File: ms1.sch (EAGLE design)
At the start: 149 parts, among them IC1 MAX3232EUE, IC2 MAX3380EEUP, J1 POWERPOLE_POWER25A, J10 Radio, J11 A3, J12 A4, J13 A5, J14 A6, J15 A7, J16 D1, J17 D2, J18 D3, J19 D4, J2 ON, J20 D5, J21 D6, J22 D7, J3 LED-EN, J4 RS232, J5 RS485, J6 A1, J7 I2C, J8 A2, J9 TTL_SERIAL, Q1 DMG6602SVT, Q2 DMG6602SVT, Q3 DMG6602SVT, Q4 DMG6602SVT, U1 LT1934ES6TRMPBF, U2 LT1934ES6TRMPBF, U3 DS3231SN, U4 ISL3179EIBZ, X1 KUSBVX-BS1N

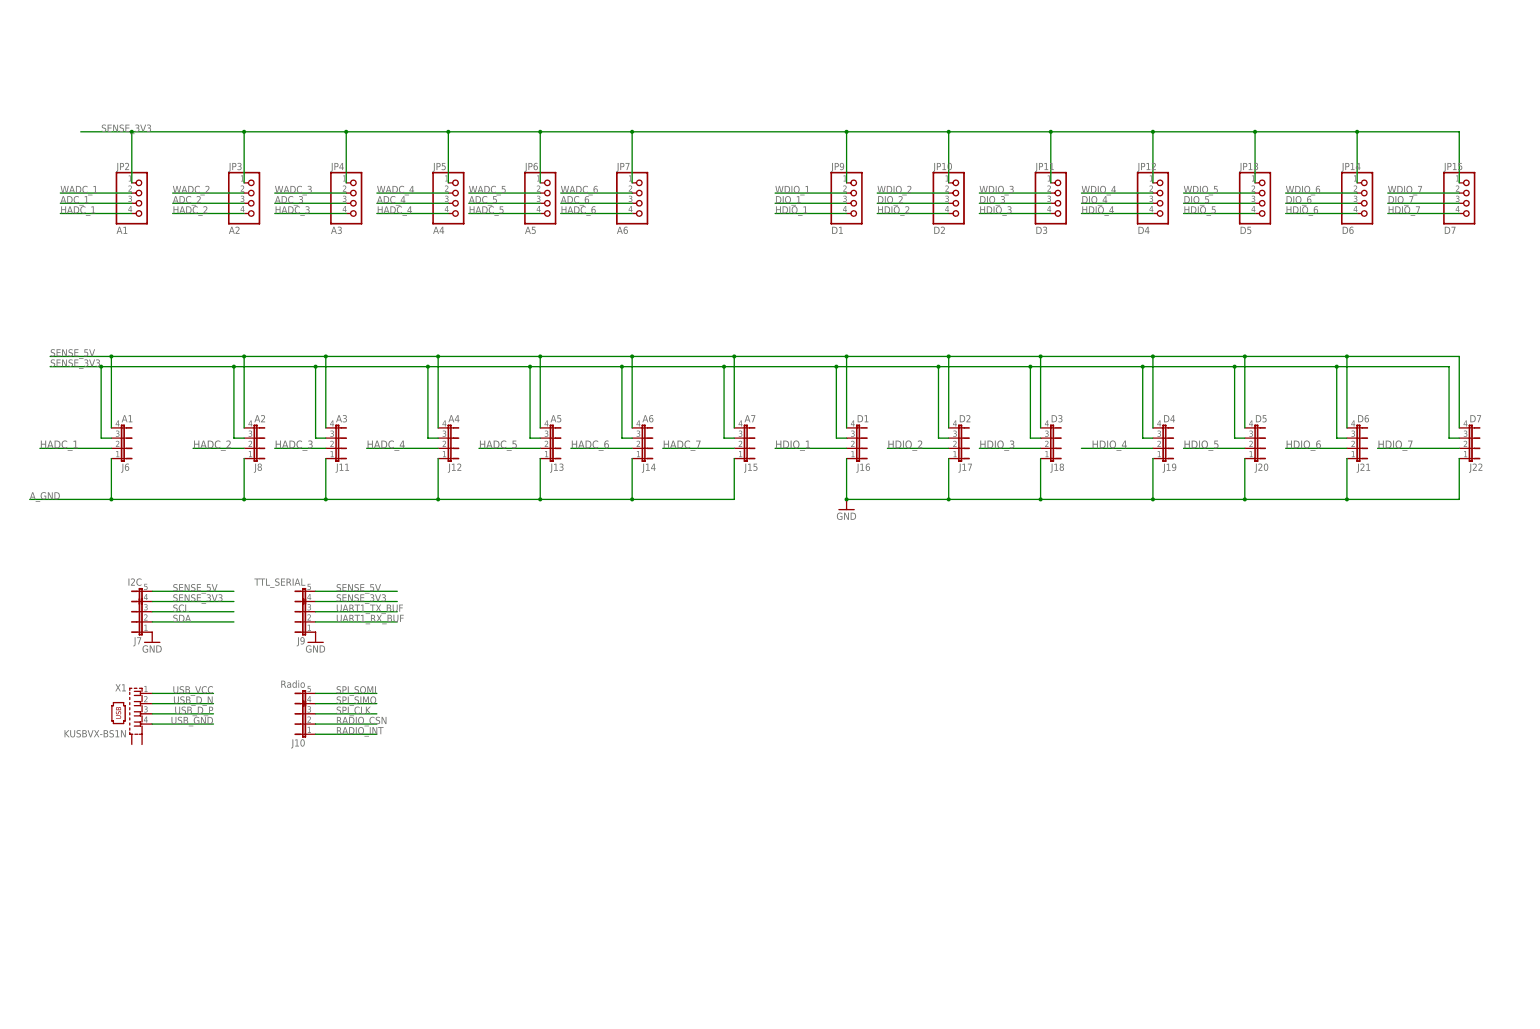
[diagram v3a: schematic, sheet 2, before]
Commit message: now uses correct serial buffer
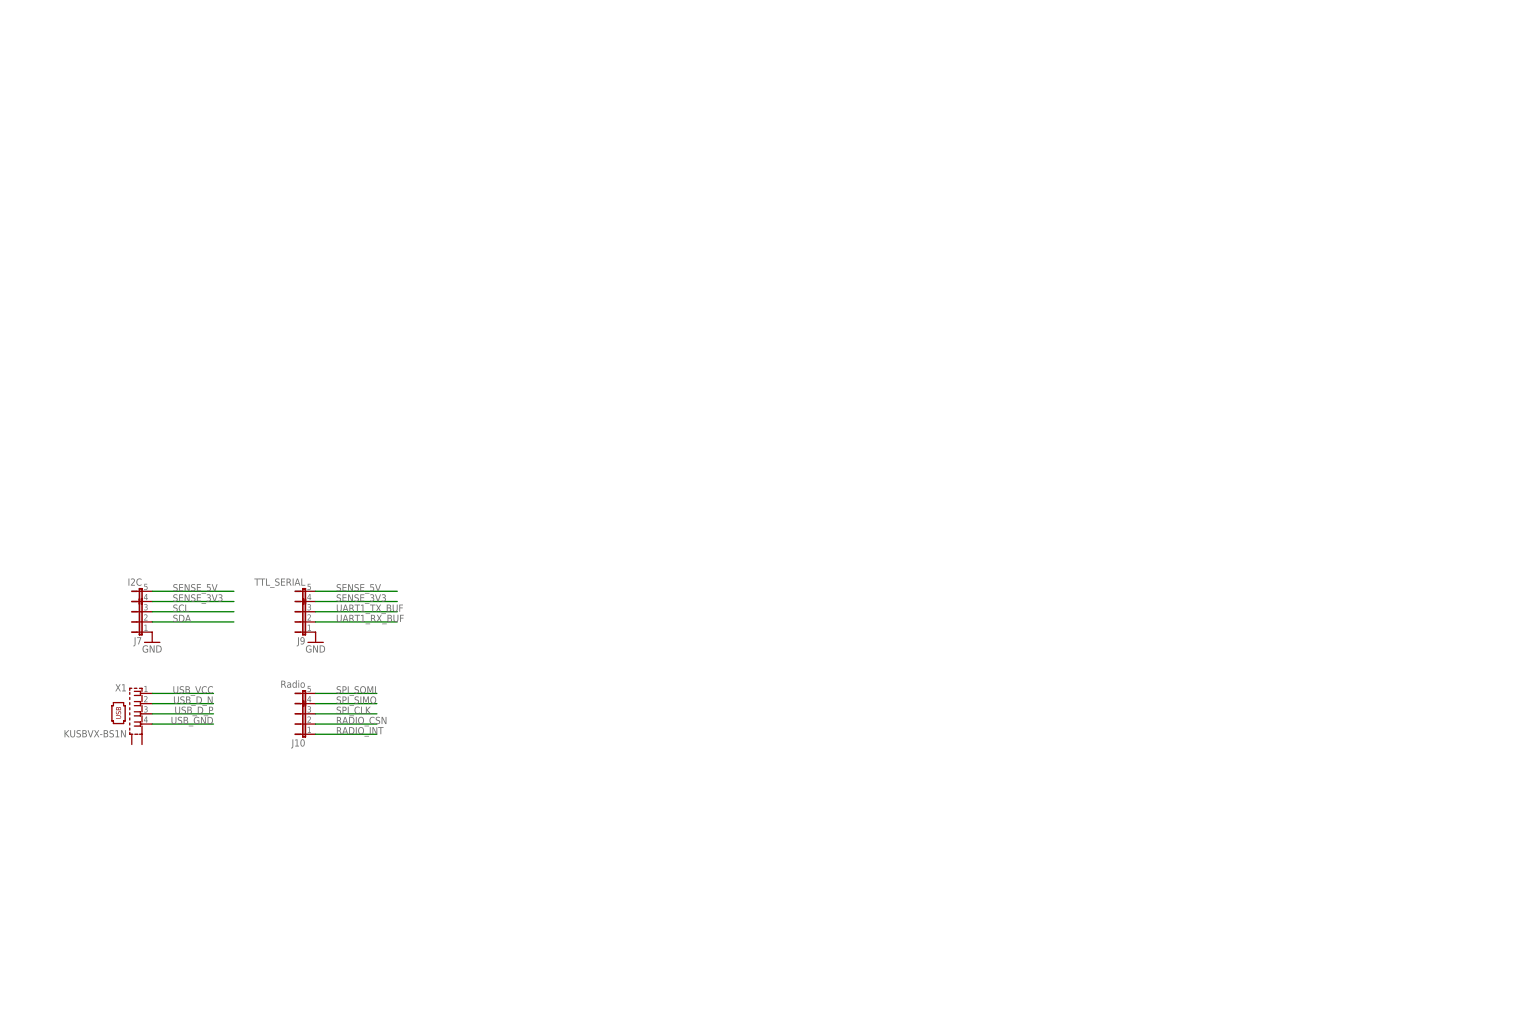
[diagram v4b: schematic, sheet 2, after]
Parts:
- removed C17, C18, C22, C23: 0.1uF, resistor:CPOL-EUA/3216-18W
- removed C26: 100nF, resistor:C-EUC0805
- removed IC2: MAX3380EEUP, basestation:MAX3380EEUP
- removed J11: A3, farnell-parts:4-PIN-MOLEX
- removed J12: A4, farnell-parts:4-PIN-MOLEX
- removed J13: A5, farnell-parts:4-PIN-MOLEX
- removed J14: A6, farnell-parts:4-PIN-MOLEX
- removed J15: A7, farnell-parts:4-PIN-MOLEX
- removed J16: D1, farnell-parts:4-PIN-MOLEX
- removed J17: D2, farnell-parts:4-PIN-MOLEX
- removed J18: D3, farnell-parts:4-PIN-MOLEX
- removed J19: D4, farnell-parts:4-PIN-MOLEX
- removed J20: D5, farnell-parts:4-PIN-MOLEX
- removed J21: D6, farnell-parts:4-PIN-MOLEX
- removed J22: D7, farnell-parts:4-PIN-MOLEX
- removed J6: A1, farnell-parts:4-PIN-MOLEX
- removed J8: A2, farnell-parts:4-PIN-MOLEX
- removed JP10: D2, pinhead:PINHD-1X4
- removed JP11: D3, pinhead:PINHD-1X4
- removed JP12: D4, pinhead:PINHD-1X4
- removed JP13: D5, pinhead:PINHD-1X4
- removed JP14: D6, pinhead:PINHD-1X4
- removed JP15: D7, pinhead:PINHD-1X4
- removed JP3: A2, pinhead:PINHD-1X4
- removed JP4: A3, pinhead:PINHD-1X4
- removed JP5: A4, pinhead:PINHD-1X4
- removed JP6: A5, pinhead:PINHD-1X4
- removed JP7: A6, pinhead:PINHD-1X4
- removed JP9: D1, pinhead:PINHD-1X4
- removed UART1_RX, UART1_TX: TPB2,54, testpad:TPB2,54
- added R7: 47K, resistor:R-EU_R0805
- added U$4: TXS0108E, basestation:TXS0108E
- JP2: value A1 -> (none); device pinhead:PINHD-1X4 -> jumper:JP2E
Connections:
- removed net A_GND: J11.1, J12.1, J13.1, J14.1, J15.1, J6.1, J8.1
- removed net HADC_1: J6.2, JP2.4
- removed net HADC_2: J8.2, JP3.4
- removed net HADC_3: J11.2, JP4.4
- removed net HADC_4: J12.2, JP5.4
- removed net HADC_5: J13.2, JP6.4
- removed net HADC_6: J14.2, JP7.4
- removed net HADC_7: J15.2
- removed net HDIO_1: J16.2, JP9.4
- removed net HDIO_2: J17.2, JP10.4
- removed net HDIO_3: J18.2, JP11.4
- removed net HDIO_4: J19.2, JP12.4
- removed net HDIO_5: J20.2, JP13.4
- removed net HDIO_6: J21.2, JP14.4
- removed net HDIO_7: J22.2, JP15.4
- removed net N$64: C17.-, IC2G$1.C1-
- removed net N$82: C18.+, IC2G$1.C2+
- removed net N$83: C18.-, IC2G$1.C2-
- removed net N$84: C22.-, IC2G$1.V-
- removed net N$9: C23.+, IC2G$1.V+
- removed net WADC_1: JP2.2
- removed net WADC_2: JP3.2
- removed net WADC_3: JP4.2
- removed net WADC_4: JP5.2
- removed net WADC_5: JP6.2
- removed net WADC_6: JP7.2
- removed net WDIO_1: JP9.2
- removed net WDIO_2: JP10.2
- removed net WDIO_3: JP11.2
- removed net WDIO_4: JP12.2
- removed net WDIO_5: JP13.2
- removed net WDIO_6: JP14.2
- removed net WDIO_7: JP15.2
- new net 232_RX: IC1G$1.R1OUT, U$4.A2
- new net 232_TX: IC1G$1.T1IN, U$4.A4
- new net 323_3V3: C19.2, IC1P.VCC, JP2.3
- new net 485_3V3: C14.1, JP2.1, R32.2, U4.VCC
- new net 485_RX: U$4.A1, U4.RO
- new net 485_TX: U$4.A3, U4.DI
- net ADC_1: no longer JP2.3
- net ADC_2: no longer JP3.3
- net ADC_3: no longer JP4.3
- net ADC_4: no longer JP5.3
- net ADC_5: no longer JP6.3
- net ADC_6: no longer JP7.3
- net DIO_1: no longer JP9.3
- net DIO_2: no longer JP10.3
- net DIO_3: no longer JP11.3, U$2.CA0
- net DIO_4: no longer JP12.3
- net DIO_5: no longer JP13.3, U$2.CA1
- net DIO_6: no longer JP14.3, U$2.CA2
- net DIO_7: no longer JP15.3
- net GND: now also U$4.GND; no longer C22.+, C23.-, C26.2, IC2P.GND, J16.1, J17.1, J18.1, J19.1, J20.1, J21.1, J22.1
- net N$8: now also R7.1, U$4.OE; no longer C17.+, IC2G$1.C1+
- net SENSE_3V3: now also JP2.2, R7.2, U$4.VCCA; no longer C14.1, C19.2, IC1P.VCC, IC2G$1.VL, J11.3, J12.3, J13.3, J14.3, J15.3, J16.3, J17.3, J18.3, J19.3, J20.3, J21.3, J22.3, J6.3, J8.3, JP10.1, JP11.1, JP12.1, JP13.1, JP14.1, JP15.1, JP2.1, JP3.1, JP4.1, JP5.1, JP6.1, JP7.1, JP9.1, R32.2, U4.VCC
- net SENSE_5V: no longer J11.4, J12.4, J13.4, J14.4, J15.4, J16.4, J17.4, J18.4, J19.4, J20.4, J21.4, J22.4, J6.4, J8.4
- net UART1_RX: now also U$4.B1, U$4.B2; no longer IC2G$1.T2IN, UART1_RX.TP
- net UART1_RX_BUF: no longer IC1G$1.R1OUT, IC2G$1.T2OUT, U4.RO
- net UART1_TX: now also U$4.B3, U$4.B4; no longer IC2G$1.T1IN, UART1_TX.TP
- net UART1_TX_BUF: no longer IC1G$1.T1IN, IC2G$1.T1OUT, U4.DI
- net VCC_3V3: now also U$4.VCCB; no longer C26.1, IC2G$1.!FORCEOFF, IC2G$1.FORCEON, IC2P.VCC
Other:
- note added: "Buffer so that drivers don't draw power from comms line."
- note added: "Each one on seperate outputs so that they can be powered individually"
- note added: "Serial Driver Choice"
- note removed: "Gum Serial Level Shift"
- note removed: "I/O Patch"
- note removed: "IO"

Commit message: now has: * rain gauge input * 2 digital io * 2 analog io * poly fuses
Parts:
- removed LED3: D3, led:LEDCHIP-LED0805
- removed LED4: D4, led:LEDCHIP-LED0805
- removed LED5: D5, led:LEDCHIP-LED0805
- removed LED6: D6, led:LEDCHIP-LED0805
- removed R13, R15, R16, R17: 56, resistor:R-EU_R0805
- added J11, J12: 4-PIN-MOLEX, farnell-parts:4-PIN-MOLEX
- added J13, J14, J8: ADC2, farnell-parts:3-PIN-MOLEX
- added J6: ADC1, farnell-parts:3-PIN-MOLEX
- added R31: 100K, resistor:R-EU_R0805
- added U$5, U$6, U$7: MCF0805, farnell-parts:MCF0805
- J5: value RS485 -> 2-PIN-MOLEX; device farnell-parts:5-PIN-MOLEX -> farnell-parts:2-PIN-MOLEX
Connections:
- removed net ADC_3: U$2.ADC3
- removed net ADC_4: U$2.ADC4
- removed net ADC_5: U$2.ADC5
- removed net ADC_6: U$2.ADC6
- removed net DIO_3: R13.2
- removed net DIO_4: R15.2
- removed net DIO_5: R16.2
- removed net DIO_6: R17.2
- removed net DIO_7: R18.2
- removed net N$11: LED6.A, R17.1
- removed net N$18: LED4.A, R15.1
- removed net N$19: LED3.A, R13.1
- removed net N$21: LED5.A, R16.1
- removed net UART1_RX_BUF: J9.2
- removed net UART1_TX_BUF: J9.3
- new net N$17: J12.4, U$6.P$1
- new net N$26: J5.1, U$7.P$1
- new net N$9: J11.4, U$5.P$1
- new net RAIN: J5.2, R18.2, R31.2, U$2.CA2
- new net TTL_RX: J9.2, U$4.A3
- new net TTL_TX: J9.3, U$4.A6
- net 232_TX: now also U$4.A5; no longer U$4.A4
- net 485_TX: now also U$4.A4; no longer U$4.A3
- net ADC_1: now also J6.2
- net ADC_2: now also J8.2
- net AGND: now also J6.3, J8.3
- net DIO_1: now also J13.2, U$2.CA0, U$2.TA0
- net DIO_2: now also J14.2
- net GND: now also J11.1, J12.1, J13.3, J14.3, R31.1; no longer J5.1
- net LGND: no longer LED3.C, LED4.C, LED5.C, LED6.C
- net RS232_RXD: now also J12.2
- net RS232_TXD: now also J12.3
- net RS485_N: now also J11.2; no longer J5.2
- net RS485_P: now also J11.3; no longer J5.3
- net SENSE_3V3: now also J13.1, J14.1, J6.1, J8.1; no longer J5.4
- net SENSE_5V: now also U$5.P$2, U$6.P$2; no longer J5.6
- net UART1_RX: now also U$4.B3
- net UART1_TX: now also U$4.B5, U$4.B6; no longer U$4.B3
- net VCC_3V3: now also U$7.P$2
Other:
- note added: "Analog Inputs"
- note added: "Digital Inputs"

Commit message: now all routed :)
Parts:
- removed C29: (no value), resistor:C-EUC0805
- removed C30: (no value), resistor:CPOL-EUB/3528-21R
- removed J9: TTL_SERIAL, farnell-parts:5-PIN-MOLEX
- removed JP16, JP8: (no value), SparkFun-Passives:JUMPER-2SMD-NO
- removed L7, L8: 10mH, resistor:L-EUL3230M
- removed LED12: RADIO, led:LEDCHIP-LED0805
- removed LED13: RADIO_EN, led:LEDCHIP-LED0805
- removed LED14: BAT_EN, led:LEDCHIP-LED0805
- removed LED15: SENSE_EN, led:LEDCHIP-LED0805
- removed R30: 56, resistor:R-EU_R0805
- removed R31: 100K, resistor:R-EU_R0805
- removed R32, R33: 1K, resistor:R-EU_R0805
- removed U$1: BUTTON_CELL_NEW, gumsense:BUTTON_CELL_NEW
- removed U$2: Z1, z1:Z1
- removed U$4: TXS0108E, basestation:TXS0108E
- added C22: 0.1uF, resistor:CPOL-EUA/3216-18W
- added C23: 100nF, resistor:C-EUC0805
- added F1, F2, F4, F5, F6, F7, F8: MCF0805, farnell-parts:MCF0805
- added JP3: (no value), SparkFun-Passives:JUMPER-2SMD-NC
- added JP4: (no value), jumper:JP2E
- added L1: 47uH, farnell-parts:SRU1048
- added L2: 20uH, rcl:L-EU6000-XXX-RC
- added LED3: RAIN, led:LEDCHIP-LED0805
- added LED4: 12V, led:LEDCHIP-LED0805
- added LED5: 3V3, led:LEDCHIP-LED0805
- added LED6: SENSE, led:LEDCHIP-LED0805
- added R13: 100K, resistor:R-EU_R0805
- added R15, R16: 56, resistor:R-EU_R0805
- added R17: 560, resistor:R-EU_R0805
- added U$8: CC1120-HEADER-SMT, CC11x:CC1120-HEADER-SMT
- C1: value 2200uF -> 2.2uF; device rcl:CPOL-EUE5-13 -> resistor:C-EUC0805
- C10: value 10pF -> 1uF
- C11: value 68uF -> 100nF; device rcl:CPOL-EUE -> resistor:C-EUC0805
- C12: value 330uF -> 2.2uF; device rcl:CPOL-EUE5-8.5 -> resistor:C-EUC0805
- C13: value 100nF -> 0.22uF
- C14: value 100nF -> 10pF; device glacsweb:C-EUC0805 -> resistor:C-EUC0805
- C15: value 0.1uF -> 68uF; device resistor:CPOL-EUA/3216-18W -> rcl:CPOL-EUE
- C16: value 0.1uF -> 330uF; device resistor:CPOL-EUA/3216-18W -> rcl:CPOL-EUE5-8.5
- C2: value 2.2uF -> 0.22uF
- C20: value 0.1uF -> 100nF; device resistor:CPOL-EUA/3216-18W -> glacsweb:C-EUC0805
- C24, C25: value 100nF -> 0.1uF; device resistor:C-EUC0805 -> resistor:CPOL-EUA/3216-18W
- C3: value 0.22uF -> 2200uF; device resistor:C-EUC0805 -> rcl:CPOL-EUE5-13
- C5: value 1uF -> 100uF; device resistor:C-EUC0805 -> rcl:CPOL-EUE
- C6: value 100uF -> 330uF; device rcl:CPOL-EUE -> rcl:CPOL-EUE5-8.5
- C7: value 330uF -> (none); device rcl:CPOL-EUE5-8.5 -> resistor:C-EUC0805
- C8: value 2.2uF -> (none); device resistor:C-EUC0805 -> resistor:CPOL-EUB/3528-21R
- C9: value 0.22uF -> 100nF
- J10: value Radio -> RS485; device farnell-parts:5-PIN-MOLEX -> farnell-parts:4-PIN-MOLEX
- J11: value 4-PIN-MOLEX -> I2C; device farnell-parts:4-PIN-MOLEX -> farnell-parts:5-PIN-MOLEX
- J12: value 4-PIN-MOLEX -> TTL_SERIAL
- J13: value ADC2 -> Radio; device farnell-parts:3-PIN-MOLEX -> farnell-parts:5-PIN-MOLEX
- J14: value ADC2 -> RS232; device farnell-parts:3-PIN-MOLEX -> farnell-parts:4-PIN-MOLEX
- J2: value ON -> RAIN
- J3: value LED-EN -> ADC1; device farnell-parts:2-PIN-MOLEX -> farnell-parts:3-PIN-MOLEX
- J4: value RS232 -> ON; device farnell-parts:5-PIN-MOLEX -> farnell-parts:2-PIN-MOLEX
- J5: value 2-PIN-MOLEX -> D1; device farnell-parts:2-PIN-MOLEX -> farnell-parts:3-PIN-MOLEX
- J6: value ADC1 -> D2
- J7: value I2C -> ADC2; device farnell-parts:5-PIN-MOLEX -> farnell-parts:3-PIN-MOLEX
- J8: value ADC2 -> LED-EN; device farnell-parts:3-PIN-MOLEX -> farnell-parts:2-PIN-MOLEX
- JP1: device SparkFun-Passives:JUMPER-2SMD-NC -> SparkFun-Passives:JUMPER-2SMD-NO
- JP2: device jumper:JP2E -> SparkFun-Passives:JUMPER-2SMD-NO
- L3: value 47uH -> 10mH; device farnell-parts:SRU1048 -> resistor:L-EUL3230M
- L4: value 20uH -> 10mH; device rcl:L-EU6000-XXX-RC -> resistor:L-EUL3230M
- LED10: value SENSE -> BAT_EN
- LED11: value SENSE_5V -> SENSE_EN
- LED7: value D7 -> 5V
- LED8: value 12V -> RADIO
- LED9: value 3V3 -> RADIO_EN
- R10, R8: value 56 -> 100K
- R14, R26: value 100K -> 56
- R19: value 560 -> 56
- R2: value 100K -> 1M
- R20: value 56 -> 1M
- R21: value 56 -> 332K
- R22: value 100K -> 150
- R23: value 1M -> 56
- R24: value 332K -> 56
- R25: value 150 -> 56
- R27, R29: value 56 -> 1K
- R28: value 56 -> 47K
- R3: value 100K -> 604K
- R4: value 51K -> 100K
- R5: value 1M -> 100K
- R6: value 604K -> 100K
- R7: value 47K -> 100K
- R9: value 100K -> 51K
- U$3: value CC1120-HEADER-SMT -> BUTTON_CELL_NEW; device CC11x:CC1120-HEADER-SMT -> gumsense:BUTTON_CELL_NEW
- U$5: value MCF0805 -> Z1; device farnell-parts:MCF0805 -> z1:Z1
- U$6: value MCF0805 -> TXS0108E; device farnell-parts:MCF0805 -> basestation:TXS0108E
- renumbered C27 to C17, C28 to C18, U$7 to F3
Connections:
- new net N$11: F4.P$1, J12.4
- new net N$18: F1.P$2, J3.1
- new net N$19: F2.P$2, J7.1
- new net N$21: F7.P$2, J6.1
- new net N$22: F8.P$2, J5.1
- net 232_RX: now also U$6.A2; no longer U$4.A2
- net 232_TX: now also U$6.A5; no longer U$4.A5
- net 323_3V3: now also C23.2, JP4.3; no longer C19.2, JP2.3
- net 485_3V3: now also C20.1, JP4.1, R27.2; no longer C14.1, JP2.1, R32.2
- net 485_RX: now also U$6.A1; no longer U$4.A1
- net 485_TX: now also U$6.A4; no longer U$4.A4
- net ADC_1: now also J3.2, U$5.ADC1; no longer J6.2, U$2.ADC1
- net ADC_2: now also J7.2, U$5.ADC2; no longer J8.2, U$2.ADC2
- net ADC_7: now also C10.1, R8.1, R9.2, U$5.ADC7; no longer C5.1, R3.1, R4.2, U$2.ADC7
- net AGND: now also C10.2, J3.3, J7.3, R9.1, U$5.AGND; no longer C5.2, J6.3, J8.3, R4.1, U$2.AGND
- net BATV_EN: now also JP3.2, R25.2, R4.2; no longer JP1.2, R1.2, R29.2
- net DC_IN: now also J4.2, R5.2; no longer J2.2, R2.2
- net DIO_1: now also J5.2, R14.2, U$5.TA0; no longer J13.2, R8.2, U$2.CA0, U$2.TA0
- net DIO_2: now also J6.2, R15.2, U$5.CA0; no longer J14.2, R10.2
- net GND: now also C1.2, C12.2, C15.-, C16.-, C20.2, C23.1, C24.-, C25.+, C3.-, C5.-, C7.2, C8.-, C9.2, J10.1, J14.1, J5.3, J6.3, J8.1, L4.2, R10.1, R21.1, R3.1, R4.1, U$3.GND, U$5.DGND, U$6.GND; no longer C1.-, C11.-, C12.-, C13.1, C14.2, C2.2, C20.-, C21.+, C24.2, C29.2, C30.-, C7.-, C8.2, J13.3, J14.3, J3.1, J4.1, J7.1, J9.1, L8.2, R22.1, R24.1, R31.1, R9.1, U$1.GND, U$2.DGND, U$4.GND
- net LGND: now also J8.2, LED3.C, LED4.C, LED5.C, LED6.C; no longer J3.2, LED12.C, LED13.C, LED14.C, LED15.C
- net N$1: now also J4.1; no longer J2.1
- net N$10: now also R27.1; no longer R32.1
- net N$107: now also C5.+, L1.P$2, L2.1, R2.2; no longer C6.+, L3.P$2, L4.1, R5.2
- net N$108: now also LED8.A, R23.1; no longer LED12.A, R27.1
- net N$109: now also LED7.A, R22.1; no longer LED11.A, R25.1
- net N$110: now also LED6.A, R19.1; no longer LED10.A, R21.1
- net N$111: now also LED5.A, R18.1; no longer LED9.A, R20.1
- net N$117: now also C2.1; no longer C3.1
- net N$118: now also R2.1, R3.2; no longer R5.1, R6.2
- net N$12: now also R5.1; no longer R2.1
- net N$13: now also C6.+, C7.1, C8.+, JP1.2, L2.2; no longer C29.1, C30.+, C7.+, JP16.2, L4.2
- net N$14: now also C16.+, JP2.1; no longer C12.+, JP8.1
- net N$15: now also LED9.A, R24.1; no longer LED13.A, R28.1
- net N$16: now also LED3.A, R16.1; no longer LED7.A, R18.1
- net N$17: now also F6.P$1, J14.4; no longer J12.4, U$6.P$1
- net N$2: now also LED4.A, R17.1; no longer LED8.A, R19.1
- net N$20: now also R15.1; no longer R10.1
- net N$23: now also R14.1; no longer R8.1
- net N$24: now also C9.1, L3.2, Q2G$2.D; no longer C24.1, L7.2, Q3G$2.D
- net N$25: now also Q3G$1.D@1, Q3G$2.G; no longer Q2G$1.D@1, Q2G$2.G
- net N$26: now also J2.1; no longer J5.1
- net N$3: now also C13.2; no longer C9.2
- net N$4: now also C13.1; no longer C9.1
- net N$5: now also C14.2, R20.1, R21.2; no longer C10.2, R23.1, R24.2
- net N$50: now also LED10.A, R25.1; no longer LED14.A, R29.1
- net N$51: now also LED11.A, R26.1; no longer LED15.A, R30.1
- net N$59: now also C22.-; no longer C16.-
- net N$6: now also C14.1, C15.+, R20.2; no longer C10.1, C11.+, R23.2
- net N$7: now also Q2G$1.D@1, Q2G$2.G, R7.1; no longer Q3G$1.D@1, Q3G$2.G, R14.1
- net N$70: now also R13.1; no longer R26.1
- net N$78: now also C2.2, L1.P$1; no longer C3.2, L3.P$1
- net N$8: now also R28.1, U$6.OE; no longer R7.1, U$4.OE
- net N$80: now also C22.+; no longer C16.+
- net N$81: now also C21.-; no longer C15.-
- net N$85: now also C21.+; no longer C15.+
- net N$86: now also C24.+; no longer C20.+
- net N$87: now also C25.-; no longer C21.-
- net N$9: now also F5.P$1, J10.4; no longer J11.4, U$5.P$1
- net RADIO_!RST: now also R29.1, U$5.CA6, U$8.!RESET; no longer R33.1, U$2.CA6, U$3.!RESET
- net RADIO_3V3: now also C11.1, L3.1, R23.2, R29.2, U$8.3V3; no longer C25.1, L7.1, R27.2, R33.2, U$3.3V3
- net RADIO_CCA_STATUS: now also U$5.TB3, U$8.GPIO3; no longer U$2.TB3, U$3.GPIO3
- net RADIO_CSN: now also J13.2, U$5.CA3, U$8.CSN; no longer J10.2, U$2.CA3, U$3.CSN
- net RADIO_EN: now also Q2G$1.G, R24.2, R6.2, U$5.TB2; no longer Q3G$1.G, R12.2, R28.2, U$2.TB2
- net RADIO_INT: now also J13.1, U$5.CAOUT, U$8.GPIO0; no longer J10.1, U$2.CAOUT, U$3.GPIO0
- net RAIN: now also J2.2, R1.2, R16.2, U$5.CA2; no longer J5.2, R18.2, R31.2, U$2.CA2
- net RGND: now also C11.2, L4.1, U$8.GND; no longer C25.2, L8.1, U$3.GND
- net RS232_RXD: now also J14.2; no longer J12.2, J4.2
- net RS232_TXD: now also J14.3; no longer J12.3, J4.3
- net RS485_N: now also J10.2; no longer J11.2
- net RS485_P: now also J10.3; no longer J11.3
- net SCL: now also J11.3, U$5.I2C_SCL; no longer J7.3, U$2.I2C_SCL
- net SDA: now also J11.2, U$5.I2C_SDA; no longer J7.2, U$2.I2C_SDA
- net SENSE_3V3: now also F1.P$1, F2.P$1, F7.P$1, F8.P$1, J11.4, JP4.2, R19.2, R28.2, U$6.VCCA; no longer J13.1, J14.1, J4.4, J6.1, J7.4, J8.1, J9.4, JP2.2, R21.2, R7.2, U$4.VCCA
- net SENSE_5V: now also F4.P$2, F5.P$2, F6.P$2, J11.6, JP2.2, R22.2; no longer J4.6, J7.6, J9.6, JP8.2, R25.2, U$5.P$2, U$6.P$2
- net SENSE_EN: now also JP3.1, Q3G$1.G, R10.2, R12.2, R26.2, U$5.TB0; no longer JP1.1, Q2G$1.G, R22.2, R30.2, R9.2, U$2.TB0
- net SPI_CLK: now also J13.3, U$5.SPI_CLK, U$8.SCLK; no longer J10.3, U$2.SPI_CLK, U$3.SCLK
- net SPI_SIMO: now also J13.4, U$5.SPI_SIMO, U$8.MOSI; no longer J10.4, U$2.SPI_SIMO, U$3.MOSI
- net SPI_SOMI: now also J13.6, U$5.SPI_SOMI, U$8.MISO; no longer J10.6, U$2.SPI_SOMI, U$3.MISO
- net TTL_RX: now also J12.2, U$6.A3; no longer J9.2, U$4.A3
- net TTL_TX: now also J12.3, U$6.A6; no longer J9.3, U$4.A6
- net UART0_RX: now also U$5.UART0_RX; no longer U$2.UART0_RX
- net UART0_TX: now also U$5.UART0_TX; no longer U$2.UART0_TX
- net UART1_RX: now also U$5.UART1_RX, U$6.B1, U$6.B2, U$6.B3; no longer U$2.UART1_RX, U$4.B1, U$4.B2, U$4.B3
- net UART1_TX: now also U$5.UART1_TX, U$6.B4, U$6.B5, U$6.B6; no longer U$2.UART1_TX, U$4.B4, U$4.B5, U$4.B6
- net USB_D_N: now also U$5.D_N; no longer U$2.D_N
- net USB_D_P: now also U$5.D_P; no longer U$2.D_P
- net USB_GND: now also U$5.USBGND; no longer U$2.USBGND
- net USB_VCC: now also U$5.USB-5V; no longer U$2.USB-5V
- net VBAT_B: now also U$3.V+@1, U$3.V+@2; no longer U$1.V+@1, U$1.V+@2
- net VCC: now also C1.1, C3.+, Q3G$2.S, R17.2; no longer C1.+, C2.1, Q2G$2.S, R19.2
- net VCC_3V3: now also C19.2, JP1.1, Q2G$2.S, R13.2, R18.2, R7.2, U$5.D-3V, U$6.VCCB; no longer C13.2, JP16.1, Q3G$2.S, R14.2, R20.2, R26.2, U$2.D-3V, U$4.VCCB
- net VCC_HP2_SW: now also C12.1, Q3G$2.D; no longer C8.1, Q2G$2.D
- net VCC_HP2_SW1: now also R8.2; no longer R3.2

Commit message: silk screen worked
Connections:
- removed net 323_3V3: C23.2, IC1P.VCC, JP4.3
- new net 232_3V3: C23.2, IC1P.VCC, JP4.1
- net 485_3V3: now also JP4.3; no longer JP4.1
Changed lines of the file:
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@@
-</segment>
-</net>
-<net name="323_3V3" class="0">
-<segment>
-<wire x1="180.34" y1="129.54" x2="157.48" y2="129.54" width="0.1524" layer="91"/>
-<wire x1="182.88" y1="127" x2="180.34" y2="127" width="0.1524" layer="91"/>
-<wire x1="180.34" y1="127" x2="180.34" y2="129.54" width="0.1524" layer="91"/>
-<junction x="180.34" y="129.54"/>
-<label x="157.48" y="129.54" size="1.778" layer="95"/>
-<pinref part="IC1" gate="P" pin="VCC"/>
-<pinref part="C23" gate="G$1" pin="2"/>
-</segment>
-<segment>
-<pinref part="JP4" gate="1" pin="3"/>
-<wire x1="190.5" y1="180.34" x2="170.18" y2="180.34" width="0.1524" layer="91"/>
-<label x="170.18" y="180.34" size="1.778" layer="95"/>
 </segment>
 </net>
@@
 </segment>
 <segment>
-<pinref part="JP4" gate="1" pin="1"/>
-<wire x1="190.5" y1="185.42" x2="170.18" y2="185.42" width="0.1524" layer="91"/>
-<label x="170.18" y="185.42" size="1.778" layer="95"/>
+<pinref part="JP4" gate="1" pin="3"/>
+<wire x1="190.5" y1="180.34" x2="170.18" y2="180.34" width="0.1524" layer="91"/>
+<label x="170.18" y="180.34" size="1.778" layer="95"/>
 </segment>
 </net>
@@
 </segment>
 </net>
+<net name="232_3V3" class="0">
+<segment>
+<pinref part="JP4" gate="1" pin="1"/>
+<wire x1="190.5" y1="185.42" x2="170.18" y2="185.42" width="0.1524" layer="91"/>
+<label x="170.18" y="185.42" size="1.778" layer="95"/>
+</segment>
+<segment>
+<wire x1="180.34" y1="129.54" x2="157.48" y2="129.54" width="0.1524" layer="91"/>
+<wire x1="182.88" y1="127" x2="180.34" y2="127" width="0.1524" layer="91"/>
+<wire x1="180.34" y1="127" x2="180.34" y2="129.54" width="0.1524" layer="91"/>
+<junction x="180.34" y="129.54"/>
+<label x="157.48" y="129.54" size="1.778" layer="95"/>
+<pinref part="IC1" gate="P" pin="VCC"/>
+<pinref part="C23" gate="G$1" pin="2"/>
+</segment>
+</net>
